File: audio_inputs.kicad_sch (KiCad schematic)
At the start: 12 parts, among them J2 AFBR-2624Z, U4 DIR9001PW, Y1 12.288 MHz

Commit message: visiually cleaned up DIR9000
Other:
- moved on the sheet: C6, C7, J2, Y1

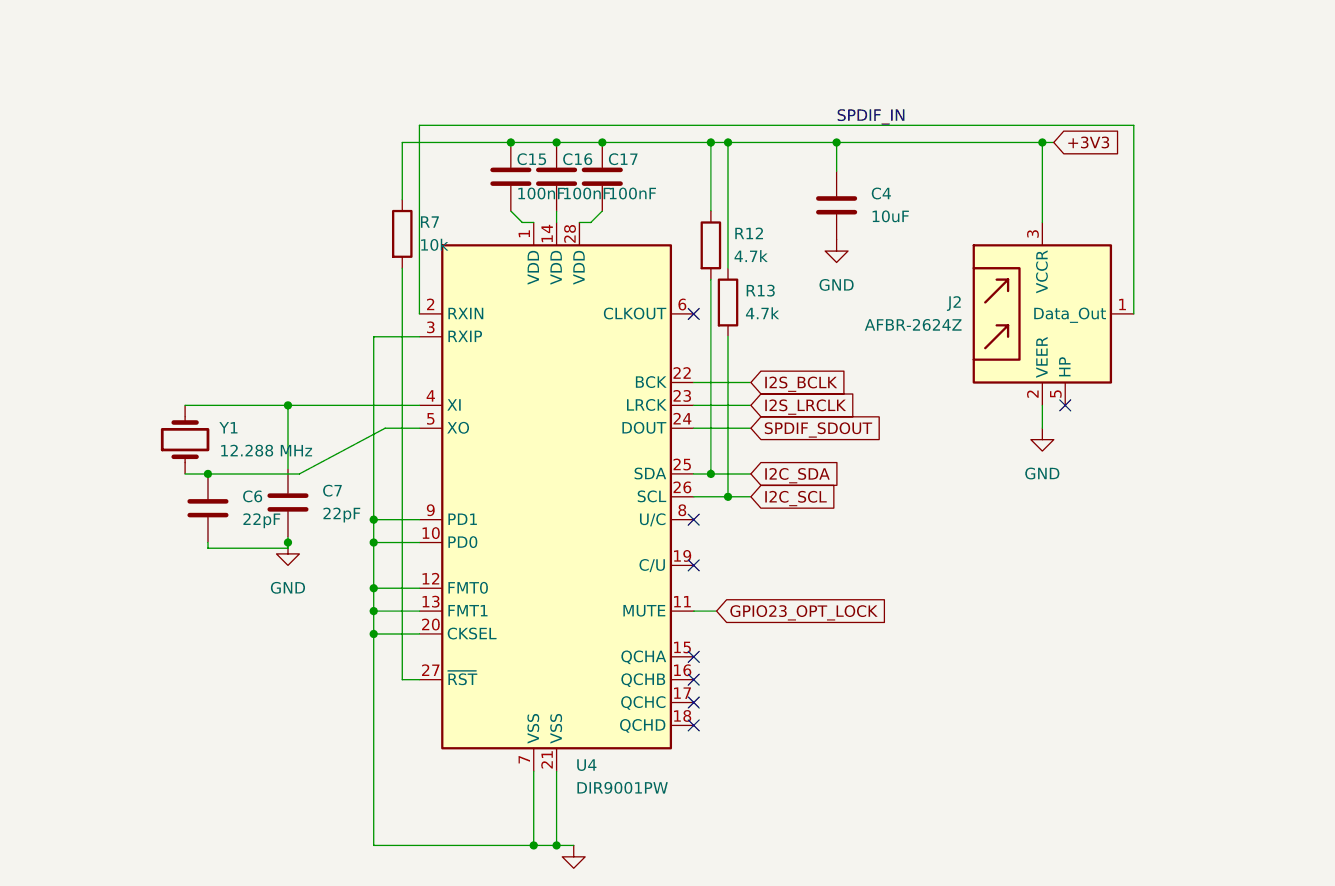
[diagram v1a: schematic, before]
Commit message: Fixed some errors, like power connections
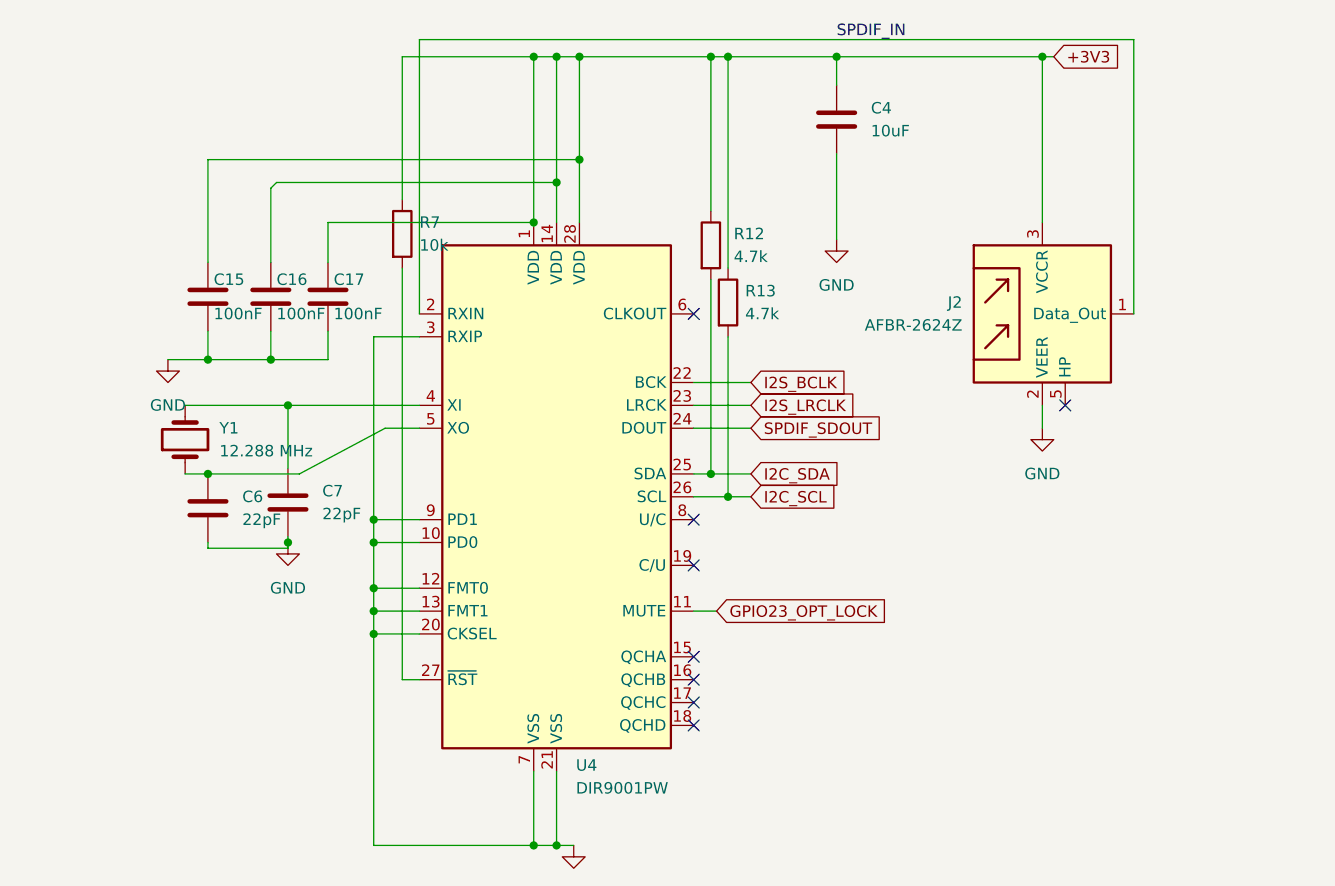
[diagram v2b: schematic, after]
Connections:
- net +3V3: now also U4.1 (VDD), U4.14 (VDD), U4.28 (VDD)
- net GND: now also C15.2, C16.2, C17.2
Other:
- moved on the sheet: C15, C16, C17, C4

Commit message: Fixed some connections and global labels
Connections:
- net I2S_BCLK renamed TOSLINK_BCLK
- net I2S_LRCLK renamed TOSLINK_LRCLK
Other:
- moved on the sheet: C15, C16, C17, C4, C6, C7, J2, Y1

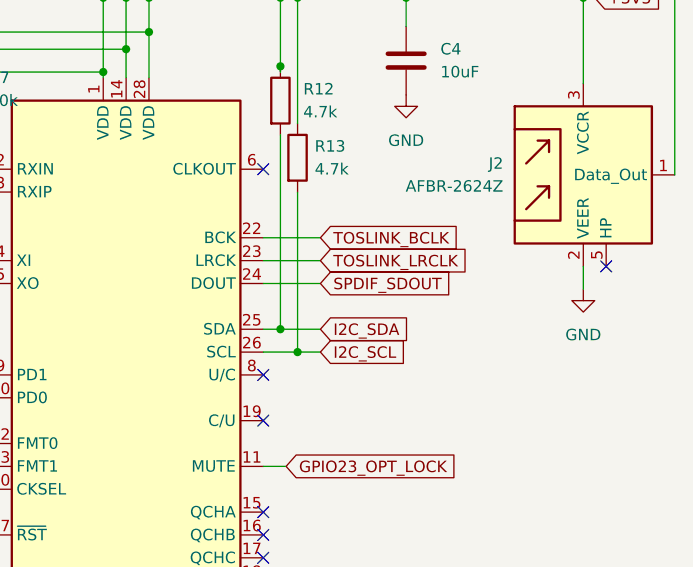
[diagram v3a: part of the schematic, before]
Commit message: Fixed power/caps for TOSLINK.  Got ERC down to warnings
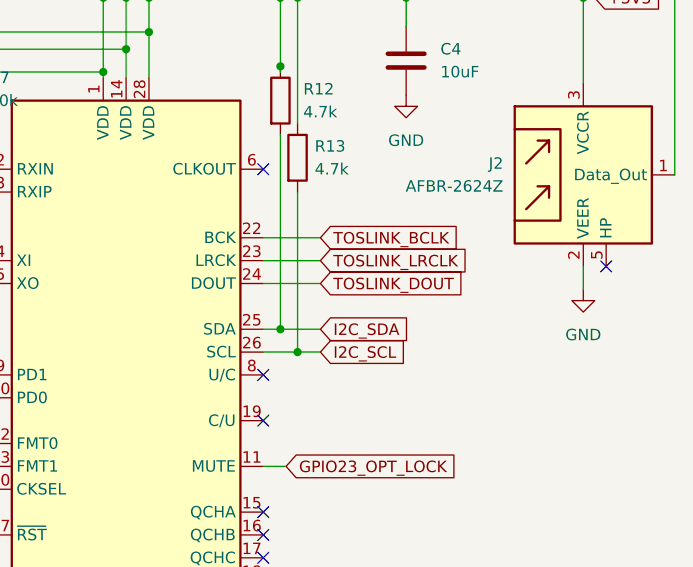
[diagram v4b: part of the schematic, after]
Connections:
- net SPDIF_SDOUT renamed TOSLINK_DOUT
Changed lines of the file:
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@@
 		)
 	)
-	(global_label "SPDIF_SDOUT"
+	(global_label "TOSLINK_DOUT"
 		(shape input)
 		(at 107.315 80.01 0)
@@
 		)
 		(property "Intersheetrefs" "${INTERSHEET_REFS}"
-			(at 122.9139 80.01 0)
+			(at 124.0025 80.01 0)
 			(effects
 				(font

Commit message: Assigned footprints that were missing
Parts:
- C15, C16, C17: footprint (none) -> Capacitor_SMD:C_0805_2012Metric_Pad1.18x1.45mm_HandSolder
- R12, R13, R7: footprint (none) -> Resistor_SMD:R_0805_2012Metric_Pad1.20x1.40mm_HandSolder
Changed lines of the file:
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@@
 			)
 		)
-		(property "Footprint" ""
+		(property "Footprint" "Capacitor_SMD:C_0805_2012Metric_Pad1.18x1.45mm_HandSolder"
 			(at 54.9402 66.04 0)
 			(effects
@@
 			)
 		)
-		(property "Footprint" ""
+		(property "Footprint" "Resistor_SMD:R_0805_2012Metric_Pad1.20x1.40mm_HandSolder"
 			(at 66.802 58.42 90)
 			(effects
@@
 			)
 		)
-		(property "Footprint" ""
+		(property "Footprint" "Capacitor_SMD:C_0805_2012Metric_Pad1.18x1.45mm_HandSolder"
 			(at 60.0202 66.04 0)
 			(effects
@@
 			)
 		)
-		(property "Footprint" ""
+		(property "Footprint" "Capacitor_SMD:C_0805_2012Metric_Pad1.18x1.45mm_HandSolder"
 			(at 49.8602 66.04 0)
 			(effects
@@
 			)
 		)
-		(property "Footprint" ""
+		(property "Footprint" "Resistor_SMD:R_0805_2012Metric_Pad1.20x1.40mm_HandSolder"
 			(at 101.092 59.69 90)
 			(effects
@@
 			)
 		)
-		(property "Footprint" ""
+		(property "Footprint" "Resistor_SMD:R_0805_2012Metric_Pad1.20x1.40mm_HandSolder"
 			(at 102.997 66.04 90)
 			(effects

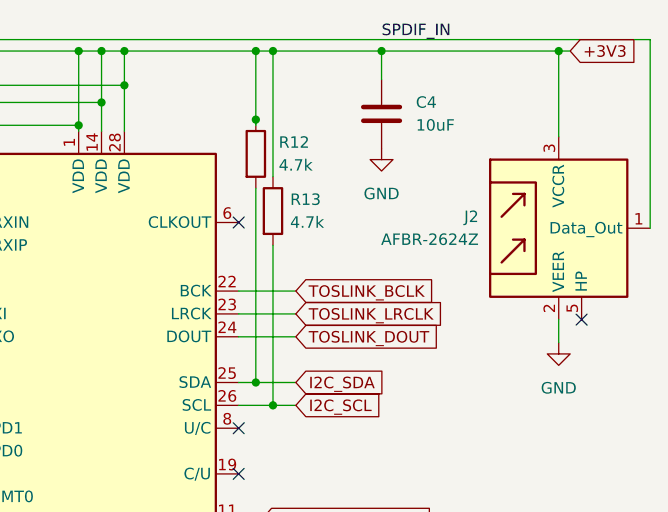
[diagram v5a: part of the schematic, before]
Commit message: Added new footprints for TOSLINK and RCA.  Fixed outer edge. PCB ready to add routes.
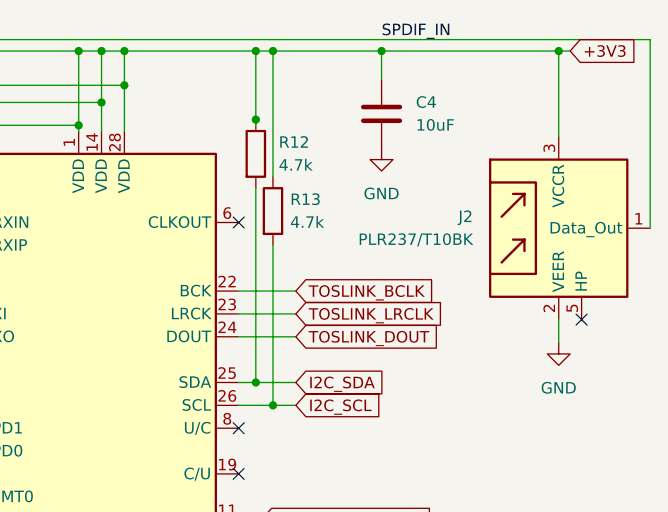
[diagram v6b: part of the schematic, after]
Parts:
- J2: value AFBR-2624Z -> PLR237/T10BK; footprint OptoDevice:Toshiba_TORX170_TORX173_TORX193_TORX194 -> Connector_Audio:PLR237-T10BK
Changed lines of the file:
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@@
 		(fields_autoplaced yes)
 		(property "Reference" "J2"
-			(at 127.635 66.6749 0)
+			(at 127 66.6749 0)
 			(effects
 				(font
@@
 			)
 		)
-		(property "Value" "AFBR-2624Z"
-			(at 127.635 69.2149 0)
+		(property "Value" "PLR237/T10BK"
+			(at 127 69.2149 0)
 			(effects
 				(font
@@
 			)
 		)
-		(property "Footprint" "OptoDevice:Toshiba_TORX170_TORX173_TORX193_TORX194"
+		(property "Footprint" "Connector_Audio:PLR237-T10BK"
 			(at 133.985 80.645 0)
 			(effects

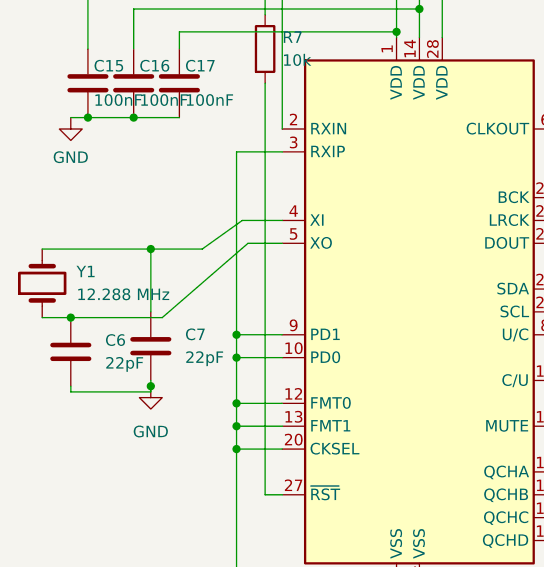
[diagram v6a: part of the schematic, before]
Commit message: Added routes for crystal and part of toslink
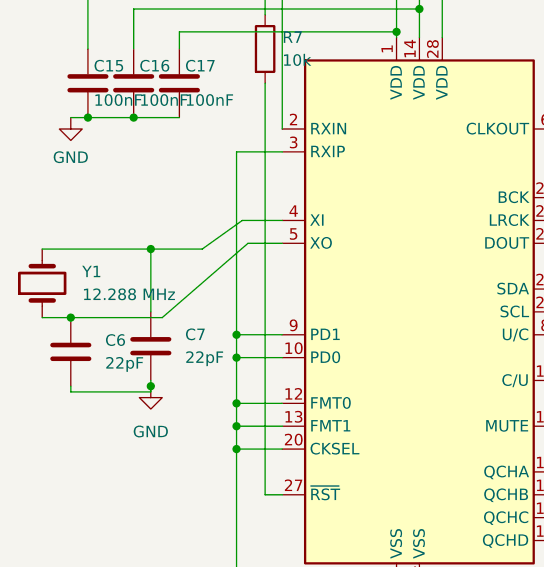
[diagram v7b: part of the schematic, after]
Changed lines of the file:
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@@
 		(fields_autoplaced yes)
 		(property "Reference" "Y1"
-			(at 47.625 83.1849 90)
+			(at 48.26 83.1849 90)
 			(effects
 				(font
@@
 		)
 		(property "Value" "12.288 MHz"
-			(at 47.625 85.7249 90)
+			(at 48.26 85.7249 90)
 			(effects
 				(font

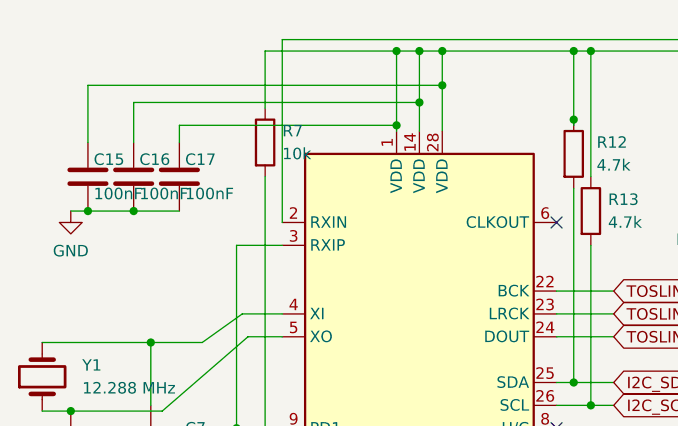
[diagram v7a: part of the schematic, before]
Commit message: Added better multiplexer setup
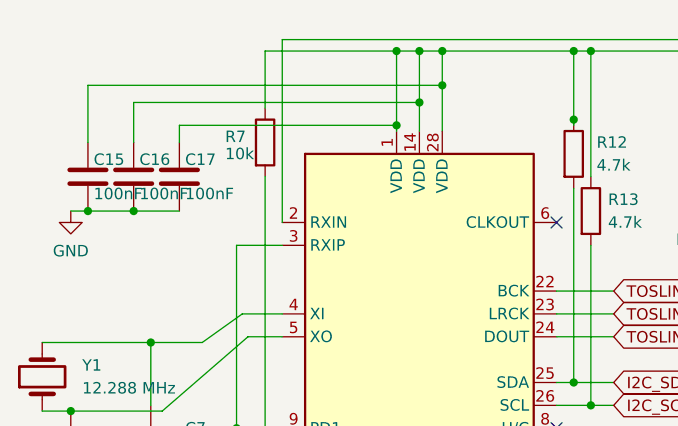
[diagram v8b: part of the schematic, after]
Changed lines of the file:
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@@
 		(on_board yes)
 		(dnp no)
-		(fields_autoplaced yes)
 		(property "Reference" "R7"
-			(at 70.485 57.1499 0)
+			(at 64.135 57.785 0)
 			(effects
 				(font
@@
 		)
 		(property "Value" "10k"
-			(at 70.485 59.6899 0)
+			(at 64.135 59.69 0)
 			(effects
 				(font
